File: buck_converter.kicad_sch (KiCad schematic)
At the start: 8 parts, among them U1 LMR516x5

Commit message: sch: first draft
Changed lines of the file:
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@@
+	)
+	(junction
+		(at 129.54 41.91)
+		(diameter 0)
+		(color 0 0 0 0)
+	)
+	(junction
+		(at 105.41 34.29)
+		(diameter 0)
+		(color 0 0 0 0)
+	)
+	(junction
+		(at 129.54 49.53)
+		(diameter 0)
+		(color 0 0 0 0)
 	)
 	(junction
@@
 	)
 	(junction
-		(at 129.54 41.91)
-		(diameter 0)
-		(color 0 0 0 0)
-	)
-	(junction
-		(at 105.41 34.29)
-		(diameter 0)
-		(color 0 0 0 0)
-	)
-	(junction
-		(at 129.54 49.53)
-		(diameter 0)
-		(color 0 0 0 0)
-	)
-	(junction
 		(at 148.59 34.29)
 		(diameter 0)
@@
 	(wire
 		(pts
+			(xy 163.83 34.29) (xy 175.26 34.29)
+		)
+		(stroke
+			(width 0)
+			(type default)
+		)
+	)
+	(wire
+		(pts
 			(xy 95.25 34.29) (xy 105.41 34.29)
 		)
@@
 		(pts
 			(xy 148.59 49.53) (xy 163.83 49.53)
-		)
-		(stroke
-			(width 0)
-			(type default)
-		)
-	)
-	(wire
-		(pts
-			(xy 163.83 34.29) (xy 171.45 34.29)
 		)
 		(stroke
@@
 	(hierarchical_label "5V"
 		(shape output)
-		(at 171.45 34.29 0)
+		(at 175.26 34.29 0)
 		(effects
 			(font

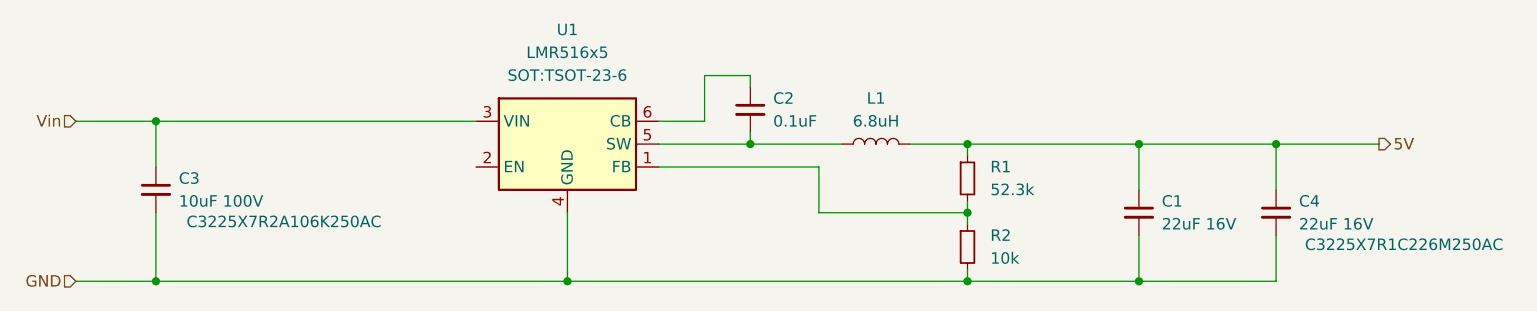
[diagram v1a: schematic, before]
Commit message: sch: fix errors
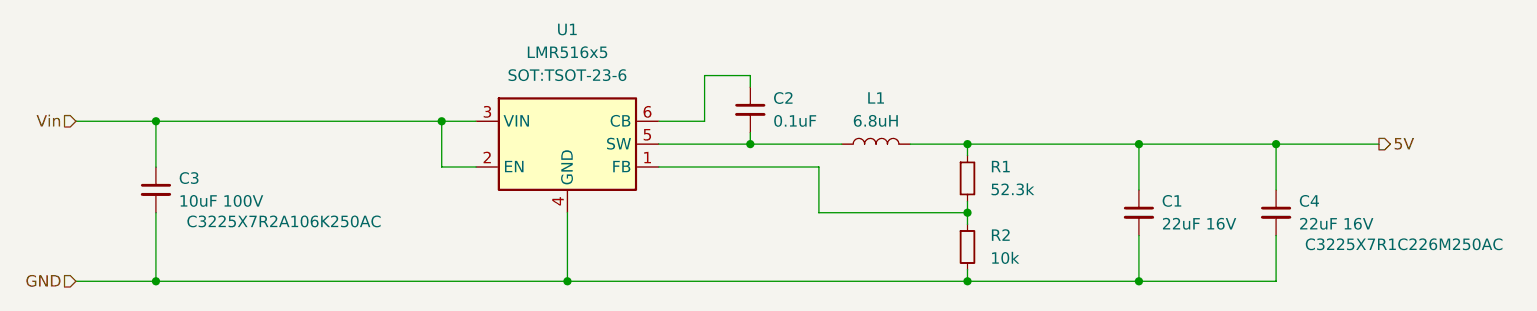
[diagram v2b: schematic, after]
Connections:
- net Vin: now also U1.2 (EN)
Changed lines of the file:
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@@
 		(color 0 0 0 0)
 	)
-	(wire
-		(pts
-			(xy 39.37 31.75) (xy 74.93 31.75)
+	(junction
+		(at 71.12 31.75)
+		(diameter 0)
+		(color 0 0 0 0)
+	)
+	(wire
+		(pts
+			(xy 39.37 31.75) (xy 71.12 31.75)
 		)
 		(stroke
@@
 	(wire
 		(pts
+			(xy 71.12 31.75) (xy 74.93 31.75)
+		)
+		(stroke
+			(width 0)
+			(type default)
+		)
+	)
+	(wire
+		(pts
 			(xy 163.83 34.29) (xy 175.26 34.29)
 		)
@@
 	(wire
 		(pts
+			(xy 74.93 36.83) (xy 71.12 36.83)
+		)
+		(stroke
+			(width 0)
+			(type default)
+		)
+	)
+	(wire
+		(pts
 			(xy 39.37 41.91) (xy 39.37 49.53)
 		)
@@
 		)
 		(stroke
+			(width 0)
+			(type default)
+		)
+	)
+	(wire
+		(pts
+			(xy 71.12 36.83) (xy 71.12 31.75)
+		)
+		(stroke
